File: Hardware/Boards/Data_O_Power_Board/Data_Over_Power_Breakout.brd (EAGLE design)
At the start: 160 x 100 mm, 22 parts, among them Y1 8Mhz

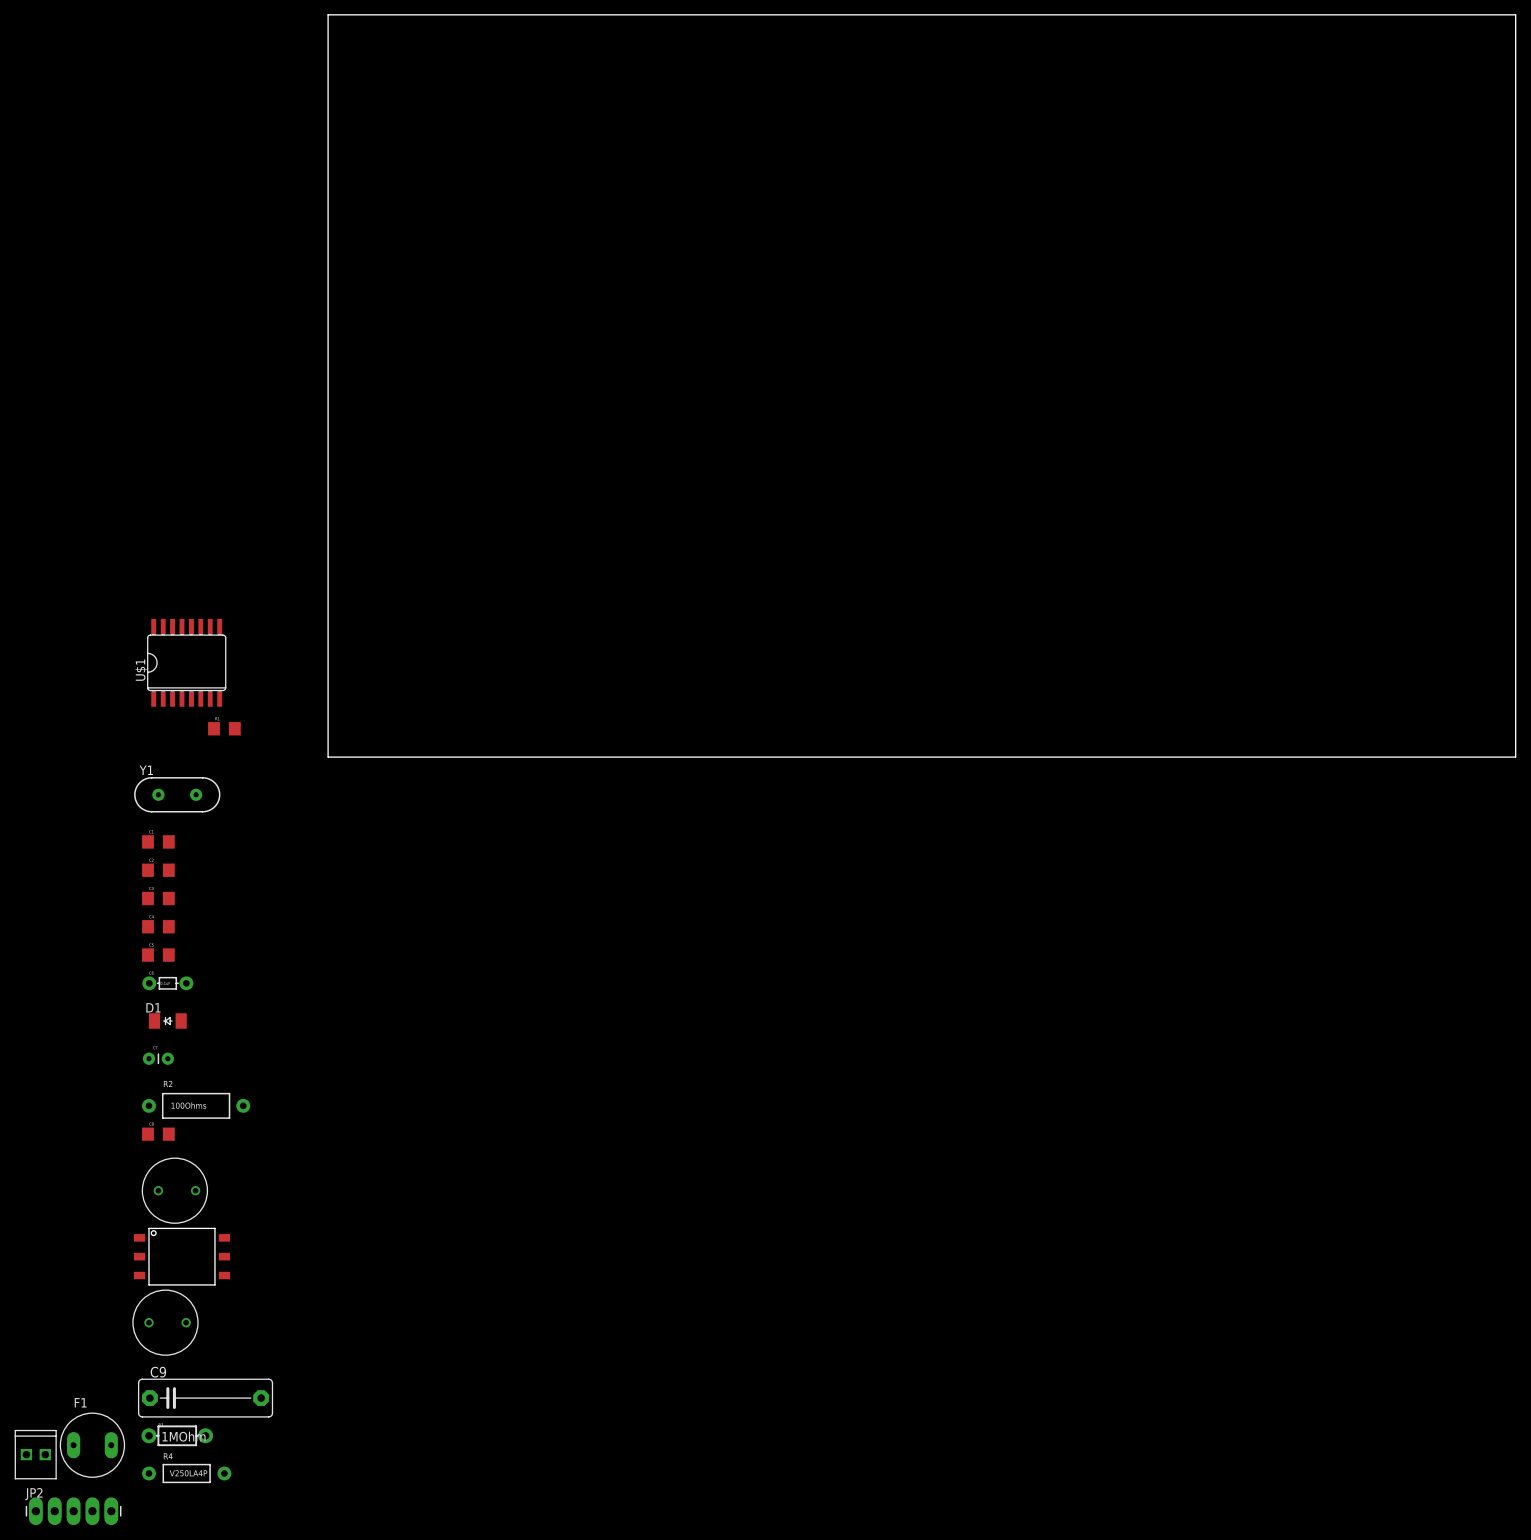
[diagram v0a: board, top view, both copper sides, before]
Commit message: Added DOP Board
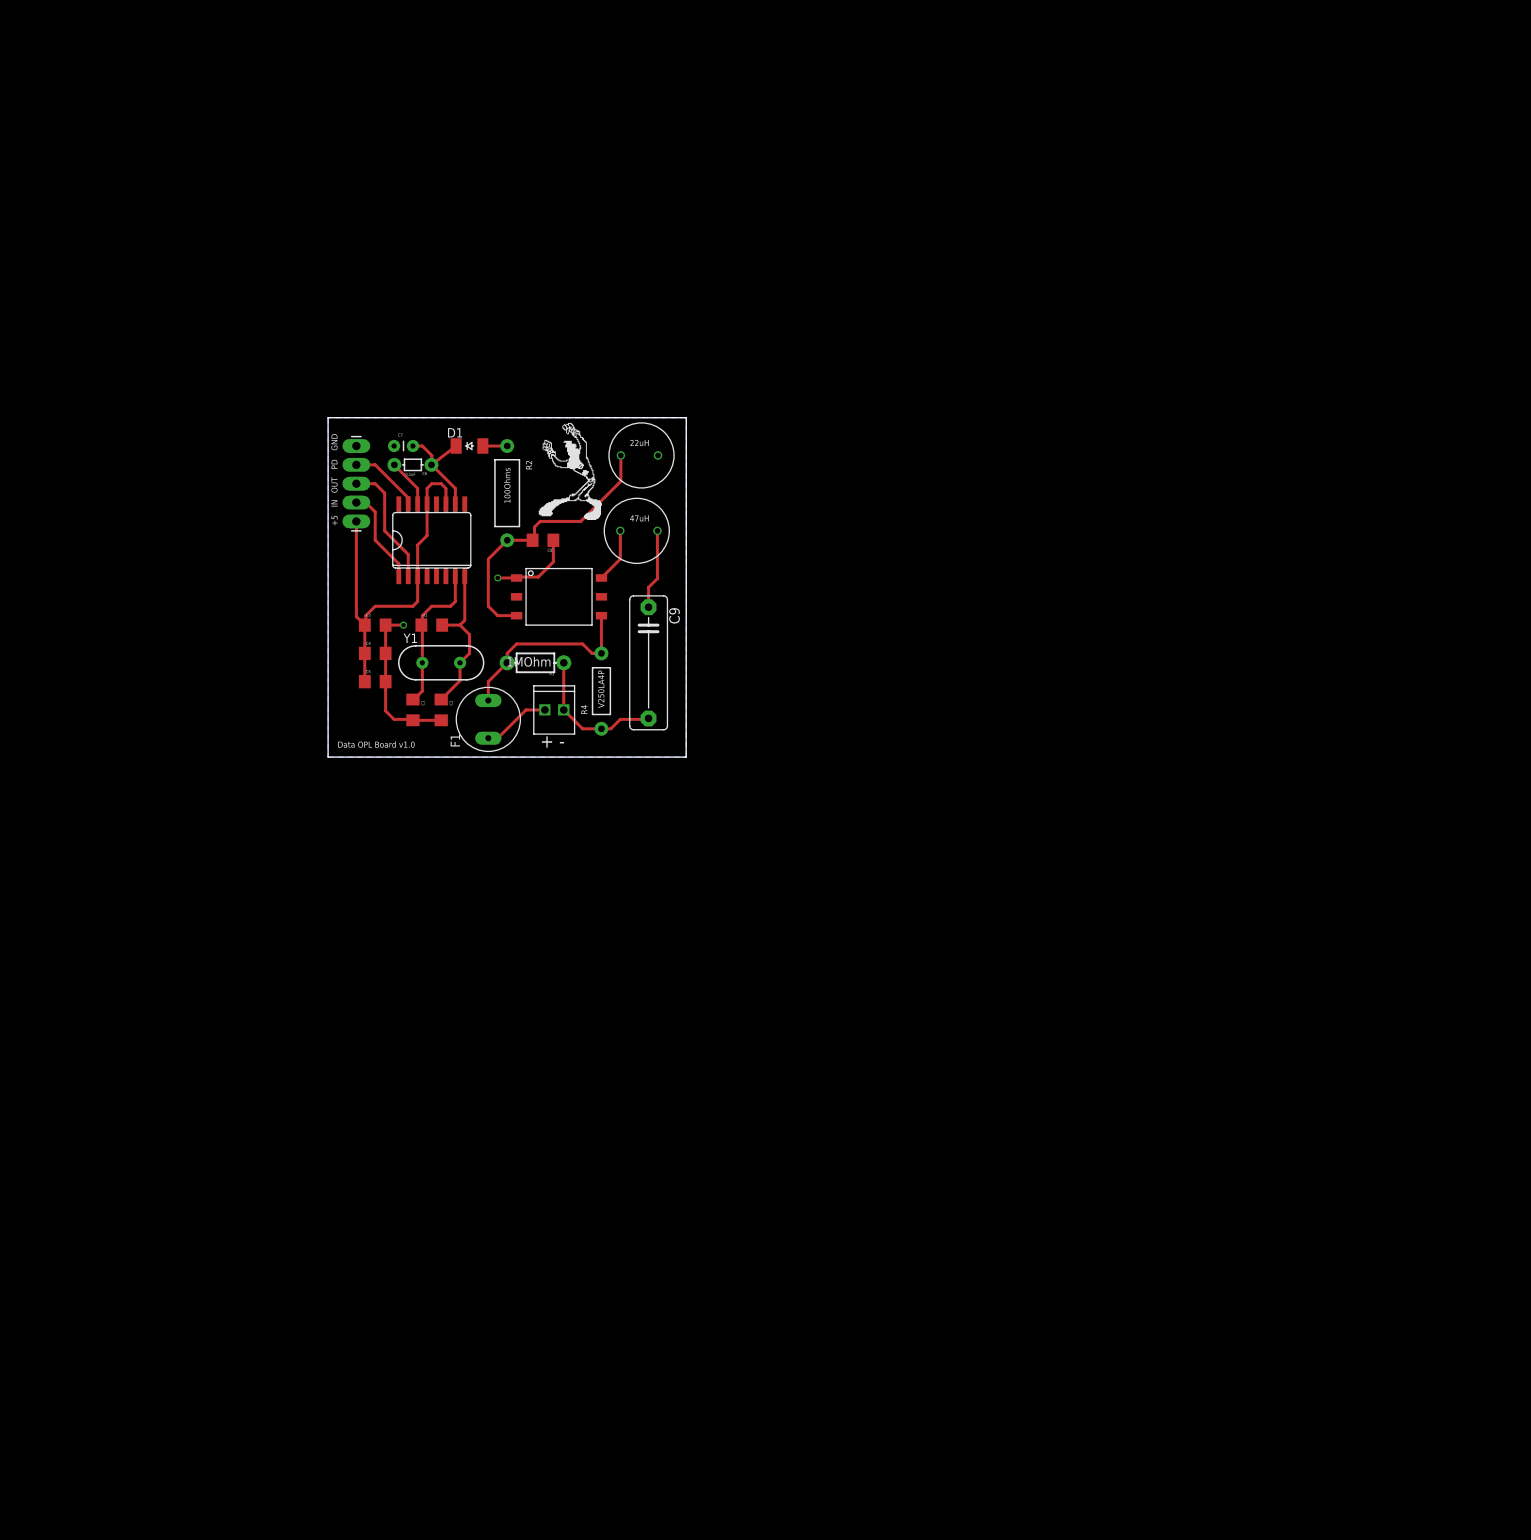
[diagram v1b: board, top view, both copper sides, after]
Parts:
- moved JP2 140.2 mm to (3.81, 31.8), turned to 90 degrees
- moved U$4 124.1 mm to (39.4, 30.5)
- moved JP1 122.3 mm to (29.2, 6.35)
- moved U$2 119.8 mm to (44.5, 40.6), turned to 180 degrees
- moved R4 119.3 mm to (36.8, 8.89), turned to 90 degrees
- moved C9 115.7 mm to (43.2, 12.7), turned to 270 degrees
- moved R3 114.8 mm to (27.9, 12.7), turned to 180 degrees
- moved F1 111.4 mm to (21.6, 5.08), turned to 90 degrees
- moved U$3 102.4 mm to (25.4, 24.1)
- moved C8 95.3 mm to (29.0, 29.2), turned to 180 degrees
- moved R2 92.6 mm to (24.1, 35.6), turned to 270 degrees
- moved C7 88.9 mm to (8.89, 41.9)
- moved D1 87.5 mm to (19.1, 41.9)
- moved C6 77.3 mm to (11.4, 39.4)
- moved C3 47.0 mm to (6.35, 17.8)
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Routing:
- net +5V: track 0.00 -> 52.1 mm
- net N$4: track 0.00 -> 37.3 mm
- net GND: track 0.00 -> 36.6 mm, vias 0 -> 2
- net N$9: track 0.00 -> 26.2 mm
- net N$1: track 0.00 -> 21.3 mm
- net N$2: track 0.00 -> 20.6 mm
- net N$8: track 0.00 -> 19.4 mm
- net N$12: track 0.00 -> 16.9 mm
- net N$6: track 0.00 -> 15.1 mm
- net N$11: track 0.00 -> 13.1 mm
- net N$7: track 0.00 -> 10.8 mm
- net N$13: track 0.00 -> 9.64 mm
- net N$10: track 0.00 -> 9.20 mm
- net N$3: track 0.00 -> 7.40 mm
- net N$5: track 0.00 -> 6.56 mm
- added copper zone on layer 16, net GND
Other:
- board size 160 x 100 mm -> 48.3 x 45.7 mm
- board text added: "+"
- board text added: "+5"
- board text added: "-"
- board text added: "22uH"
- board text added: "47uH"
- board text added: "Data OPL Board v1.0"
- board text added: "GND"
- board text added: "IN"
- board text added: "OUT"
- board text added: "PD"
